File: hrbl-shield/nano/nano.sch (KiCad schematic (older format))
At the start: 57 parts, among them P1 Digital, P2 Analog, P3 CONN_01X01, P4 CONN_01X01, P5 CONN_01X01, P6 CONN_01X01, U1 SFH6206-3T, U10 SFH6206-3T, U11 SFH6206-3T, U12 SFH6206-3T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

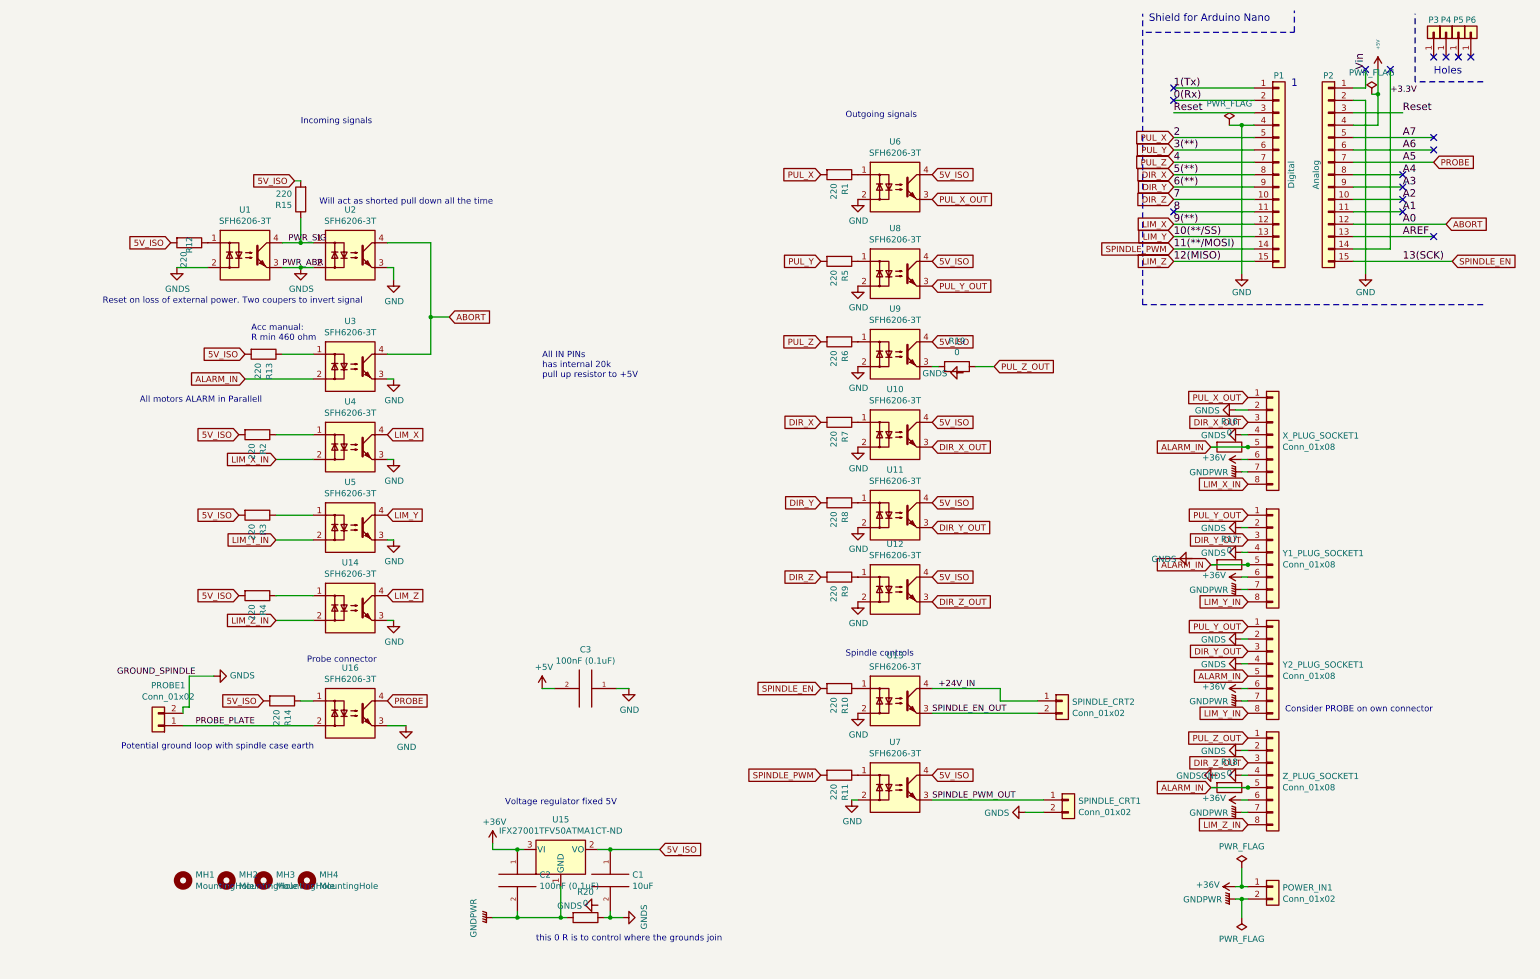
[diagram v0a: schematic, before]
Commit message: Dust skirt
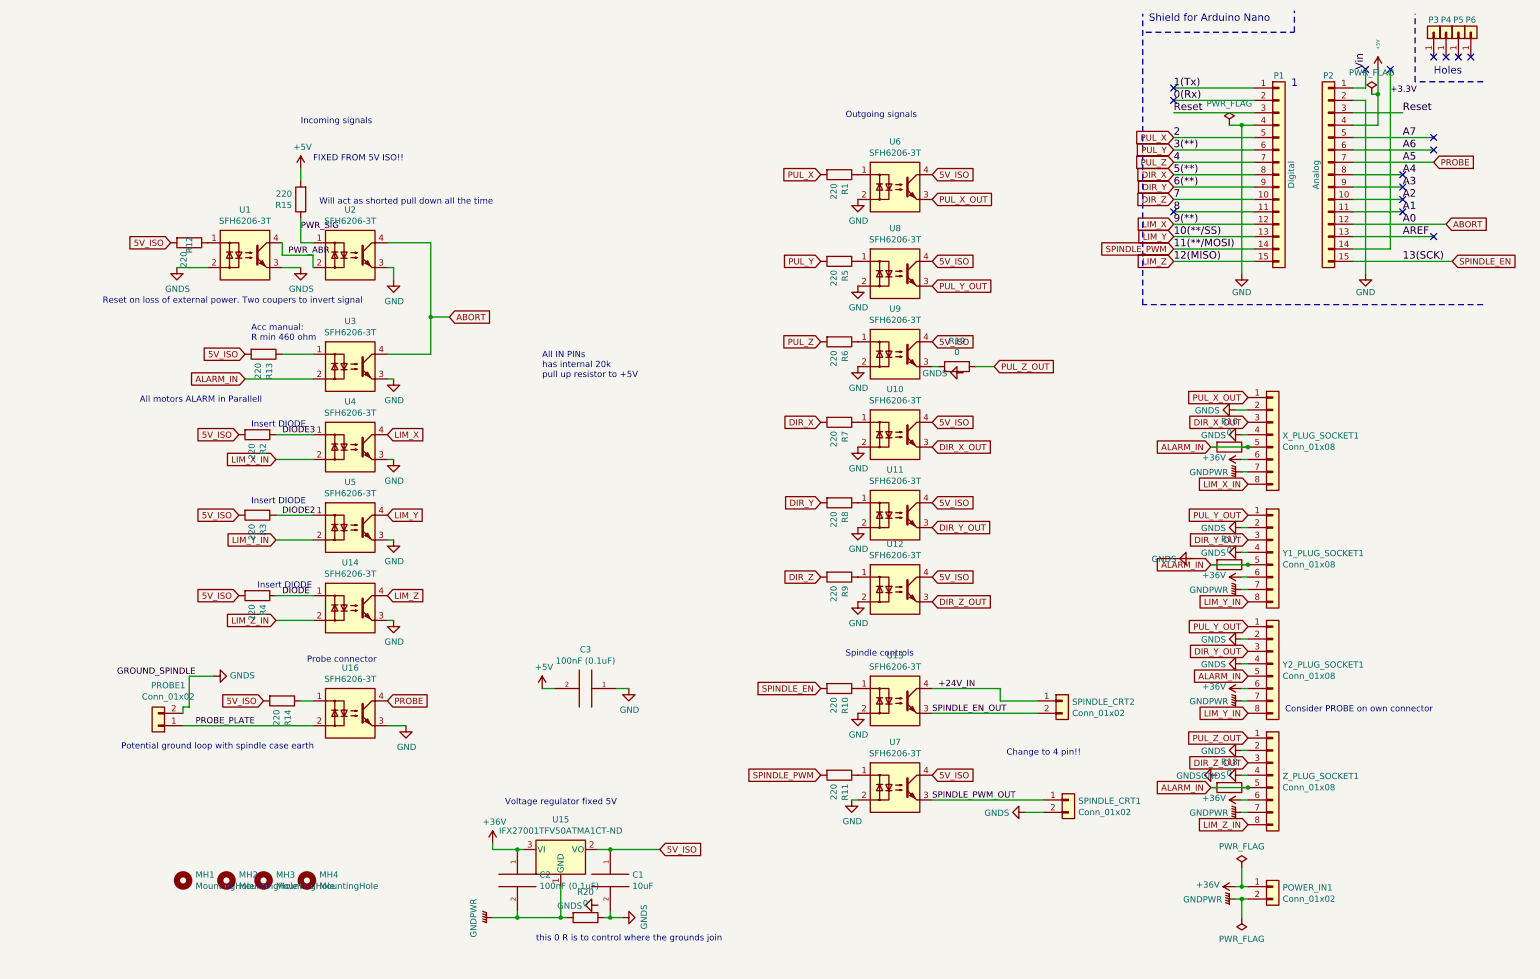
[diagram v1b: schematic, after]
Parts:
- Z_PLUG_SOCKET1: footprint Connector_Phoenix_MC:PhoenixContact_MCV_1,5_8-G-3.81_1x08_P3.81mm_Vertical -> Connector_Phoenix_MC:PhoenixContact_MCV_1,5_8-G-3.5_1x08_P3.50mm_Vertical
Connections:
- net +5V: now also R15.2
- net 5V_ISO: no longer R15.2
- net GNDS: no longer U2.2
- net PWR_SIG: no longer U1.4
- net DIODE3: now reaches R2.1, U4.1
- net DIODE2: now reaches R3.1, U5.1
- net DIODE: now reaches R4.1, U14.1
- new net PWR_ABR: U1.4, U2.2
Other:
- note added: "Change to 4 pin!!"
- note added: "FIXED FROM 5V ISO!!"
- note added: "Insert DIODE"
- note added: "Insert DIODE\n\n"
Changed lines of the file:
@@
 F 0 "Z_PLUG_SOCKET1" H 9579 6642 50  0000 L CNN
 F 1 "Conn_01x08" H 9579 6551 50  0000 L CNN
-F 2 "Connector_Phoenix_MC:PhoenixContact_MCV_1,5_8-G-3.81_1x08_P3.81mm_Vertical" H 9500 6650 50  0001 C CNN
+F 2 "Connector_Phoenix_MC:PhoenixContact_MCV_1,5_8-G-3.5_1x08_P3.50mm_Vertical" H 9500 6650 50  0001 C CNN
 F 3 "~" H 9500 6650 50  0001 C CNN
 	1    9500 6650
@@
 Wire Wire Line
 	2400 2550 2400 2650
-Text GLabel 1600 1850 0    50   Input ~ 0
-5V_ISO
 $Comp
 L Device:R R15
@@
 Acc manual: \nR min 460 ohm\n
 Wire Wire Line
-	1600 1850 1650 1850
-Wire Wire Line
 	1650 2150 1650 2350
 $Comp
@@
 $EndComp
 Wire Wire Line
-	1650 2350 1500 2350
-Wire Wire Line
 	650  2550 900  2550
 $Comp
@@
 $EndComp
 Wire Wire Line
-	1750 2550 1650 2550
-Connection ~ 1650 2550
-Wire Wire Line
 	1750 2350 1650 2350
-Connection ~ 1650 2350
 Wire Wire Line
 	2700 2350 2350 2350
@@
 Wire Wire Line
 	2350 4100 2400 4100
-Text Label 1500 2550 0    50   ~ 0
+Text Label 1550 2450 0    50   ~ 0
 PWR_ABR
-Text Label 1550 2350 0    50   ~ 0
+Text Label 1650 2250 0    50   ~ 0
 PWR_SIG
 $Comp
@@
 Wire Wire Line
 	750  5850 950  5850
+$Comp
+L power:+5V #PWR0115
+U 1 1 5B8E61E3
+P 1650 1750
+F 0 "#PWR0115" H 1650 1600 50  0001 C CNN
+F 1 "+5V" H 1665 1923 50  0000 C CNN
+F 2 "" H 1650 1750 50  0001 C CNN
+F 3 "" H 1650 1750 50  0001 C CNN
+	1    1650 1750
+	1    0    0    -1
+$EndComp
+Wire Wire Line
+	1650 1750 1650 1850
+Text Notes 1750 1700 0    50   ~ 0
+FIXED FROM 5V ISO!!
+Text Notes 7350 6500 0    50   ~ 0
+Change to 4 pin!!
+Text Notes 1300 5150 0    50   ~ 0
+Insert DIODE
+Text Notes 1250 4550 0    50   ~ 0
+Insert DIODE\n\n
+Text Notes 1250 3850 0    50   ~ 0
+Insert DIODE
+Text Label 1500 5200 0    50   ~ 0
+DIODE
+Text Label 1500 4550 0    50   ~ 0
+DIODE2
+Text Label 1500 3900 0    50   ~ 0
+DIODE3
+Wire Wire Line
+	1750 2550 1750 2450
+Wire Wire Line
+	1750 2450 1500 2450
+Wire Wire Line
+	1500 2450 1500 2350
 $EndSCHEMATC

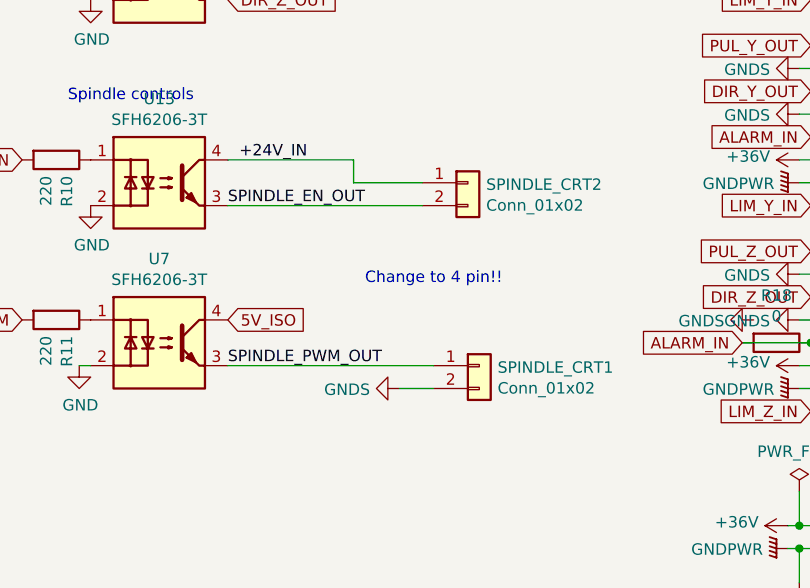
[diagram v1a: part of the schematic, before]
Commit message: corrected singals
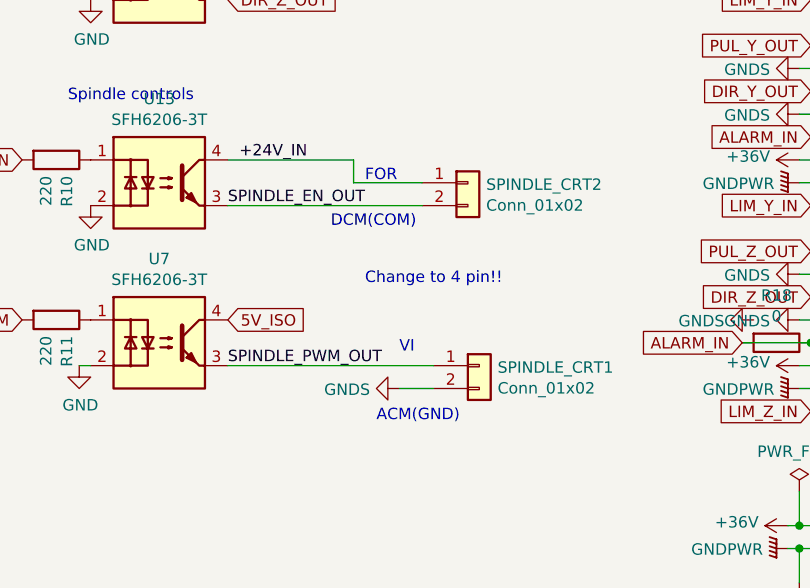
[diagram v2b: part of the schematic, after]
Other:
- note added: "ACM(GND)"
- note added: "DCM(COM)"
- note added: "FOR"
- note added: "VI\n"
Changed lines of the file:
@@
 Wire Wire Line
 	1500 2450 1500 2350
+Text Notes 7200 6250 0    50   ~ 0
+DCM(COM)
+Text Notes 7350 6050 0    50   ~ 0
+FOR
+Text Notes 7400 7100 0    50   ~ 0
+ACM(GND)
+Text Notes 7500 6800 0    50   ~ 0
+VI\n
 $EndSCHEMATC

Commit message: Shield fixes
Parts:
- removed SPINDLE_CRT1, SPINDLE_CRT2: Conn_01x02, Connector_Phoenix_MC:PhoenixContact_MCV_1,5_2-G-3.5_1x02_P3.50mm_Vertical, symbol Connector_Generic:Conn_01x02
- added J1: Conn_01x04, Connector_Phoenix_MC:PhoenixContact_MCV_1,5_4-G-3.5_1x04_P3.50mm_Vertical, symbol Connector_Generic:Conn_01x04
- added S1JA-13-F1: DIODE, Diode_SMD:D_SMA_Handsoldering, symbol pspice:DIODE
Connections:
- net 5V_ISO: now also S1JA-13-F1.1 (K); no longer R2.2, R3.2, R4.2
- net GNDS: now also J1.4 (Pin_4)
- net +24V_IN renamed FOR
- net FOR: now also J1.1 (Pin_1)
- net SPINDLE_EN_OUT renamed DCM(COM)
- net DCM(COM): now also J1.2 (Pin_2)
- net SPINDLE_PWM_OUT renamed VI
- net VI: now also J1.3 (Pin_3)
- new net: R2.2, R3.2, R4.2, S1JA-13-F1.2 (A)
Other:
- note added: "+24V in"
- note added: "Reset on loss of external power. \nTwo coupers to invert signal\n"
- note added: "Spindle PWM out"
- note added: "Spindle_EN_out"
- note added: "To stop backflow from the\n 36V pullup on the limit switch signal pin"
- note removed: "Change to 4 pin!!"
- note removed: "Reset on loss of external power. Two coupers to invert signal\n"
- note removed: "Will act as shorted pull down all the time"
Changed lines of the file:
@@
 Text Notes 6050 1350 0    50   ~ 0
 Outgoing signals
-Text Notes 1650 1400 0    50   ~ 0
-Incoming signals
 Text GLabel 2350 3900 2    50   Input ~ 0
 LIM_X
@@
 	1    2400 5400
 	1    0    0    -1
-$EndComp
-$Comp
-L Device:R R4
-U 1 1 5B816D2B
-P 1300 5200
-F 0 "R4" H 1370 5246 50  0000 L CNN
-F 1 "220" H 1370 5155 50  0000 L CNN
-F 2 "Resistor_SMD:R_1206_3216Metric_Pad1.42x1.75mm_HandSolder" V 1230 5200 50  0001 C CNN
-F 3 "~" H 1300 5200 50  0001 C CNN
-	1    1300 5200
-	0    1    1    0
 $EndComp
 $Comp
@@
 $EndComp
 Text Label 6800 5950 0    50   ~ 0
-+24V_IN
+FOR
 Text Label 6750 6150 0    50   ~ 0
-SPINDLE_EN_OUT
+DCM(COM)
 $Comp
 L power:GNDS #PWR06
 U 1 1 5B842985
-P 7500 6950
-F 0 "#PWR06" H 7500 6700 50  0001 C CNN
-F 1 "GNDS" V 7505 6822 50  0000 R CNN
-F 2 "" H 7500 6950 50  0001 C CNN
-F 3 "" H 7500 6950 50  0001 C CNN
-	1    7500 6950
+P 6800 6950
+F 0 "#PWR06" H 6800 6700 50  0001 C CNN
+F 1 "GNDS" V 6805 6822 50  0000 R CNN
+F 2 "" H 6800 6950 50  0001 C CNN
+F 3 "" H 6800 6950 50  0001 C CNN
+	1    6800 6950
 	0    1    1    0
 $EndComp
@@
 	1    0    0    -1
 $EndComp
-Text Label 6750 6850 0    50   ~ 0
-SPINDLE_PWM_OUT
 Text Notes 6050 5700 0    50   ~ 0
 Spindle controls
@@
 Text GLabel 6750 1800 2    50   Input ~ 0
 5V_ISO
-Text GLabel 1150 5200 0    50   Input ~ 0
-5V_ISO
-Text GLabel 1150 4550 0    50   Input ~ 0
-5V_ISO
-Text GLabel 1150 3900 0    50   Input ~ 0
+Text GLabel 150  4550 0    50   Input ~ 0
 5V_ISO
 Text GLabel 4550 7250 2    50   Input ~ 0
@@
 Text GLabel 2850 2950 2    50   Input ~ 0
 ABORT
-Text Notes 50   2850 0    50   ~ 0
-Reset on loss of external power. Two coupers to invert signal\n
+Text Notes 200  2950 0    50   ~ 0
+Reset on loss of external power. \nTwo coupers to invert signal\n
 Text Notes 3600 3450 0    50   ~ 0
 All IN PINs\nhas internal 20k \npull up resistor to +5V
@@
 	-1   0    0    1
 $EndComp
-Text Notes 1250 3150 0    50   ~ 0
+Text Notes 550  3400 0    50   ~ 0
 Acc manual: \nR min 460 ohm\n
 Wire Wire Line
@@
 L power:GNDS #PWR08
 U 1 1 5B9C09BB
-P 1650 2550
-F 0 "#PWR08" H 1650 2300 50  0001 C CNN
-F 1 "GNDS" H 1655 2377 50  0000 C CNN
-F 2 "" H 1650 2550 50  0001 C CNN
-F 3 "" H 1650 2550 50  0001 C CNN
-	1    1650 2550
+P 1650 2600
+F 0 "#PWR08" H 1650 2350 50  0001 C CNN
+F 1 "GNDS" H 1655 2427 50  0000 C CNN
+F 2 "" H 1650 2600 50  0001 C CNN
+F 3 "" H 1650 2600 50  0001 C CNN
+	1    1650 2600
 	1    0    0    -1
 $EndComp
@@
 Wire Wire Line
 	4200 5950 4300 5950
-Text Notes 1800 2050 0    50   ~ 0
-Will act as shorted pull down all the time
 $Comp
 L Isolator:SFH6206-3T U6
@@
 	1    0    0    -1
 $EndComp
-Wire Wire Line
-	6750 5950 7300 5950
-Wire Wire Line
-	7300 5950 7300 6050
 $Comp
 L Isolator:SFH6206-3T U7
@@
 	1    0    0    -1
 $EndComp
-$Comp
-L Connector_Generic:Conn_01x02 SPINDLE_CRT2
-U 1 1 5B881667
-P 7800 6050
-F 0 "SPINDLE_CRT2" H 7880 6042 50  0000 L CNN
-F 1 "Conn_01x02" H 7880 5951 50  0000 L CNN
-F 2 "Connector_Phoenix_MC:PhoenixContact_MCV_1,5_2-G-3.5_1x02_P3.50mm_Vertical" H 7800 6050 50  0001 C CNN
-F 3 "~" H 7800 6050 50  0001 C CNN
-	1    7800 6050
-	1    0    0    -1
-$EndComp
-$Comp
-L Connector_Generic:Conn_01x02 SPINDLE_CRT1
-U 1 1 5B887DAA
-P 7850 6850
-F 0 "SPINDLE_CRT1" H 7930 6842 50  0000 L CNN
-F 1 "Conn_01x02" H 7930 6751 50  0000 L CNN
-F 2 "Connector_Phoenix_MC:PhoenixContact_MCV_1,5_2-G-3.5_1x02_P3.50mm_Vertical" H 7850 6850 50  0001 C CNN
-F 3 "~" H 7850 6850 50  0001 C CNN
-	1    7850 6850
-	1    0    0    -1
-$EndComp
-Wire Wire Line
-	7300 6050 7600 6050
-Wire Wire Line
-	6750 6150 7600 6150
 Wire Wire Line
 	6750 6850 7650 6850
-Wire Wire Line
-	7500 6950 7650 6950
 Text Label 800  5850 2    50   ~ 0
 GROUND_SPINDLE
@@
 Text Notes 1750 1700 0    50   ~ 0
 FIXED FROM 5V ISO!!
-Text Notes 7350 6500 0    50   ~ 0
-Change to 4 pin!!
 Text Notes 1300 5150 0    50   ~ 0
 Insert DIODE
@@
 Wire Wire Line
 	1500 2450 1500 2350
-Text Notes 7200 6250 0    50   ~ 0
+Text Notes 8250 6450 0    50   ~ 0
 DCM(COM)
-Text Notes 7350 6050 0    50   ~ 0
+Text Notes 8250 6350 0    50   ~ 0
 FOR
-Text Notes 7400 7100 0    50   ~ 0
+Text Notes 8250 6650 0    50   ~ 0
 ACM(GND)
-Text Notes 7500 6800 0    50   ~ 0
+Text Notes 8250 6550 0    50   ~ 0
 VI\n
+$Comp
+L pspice:DIODE S1JA-13-F1
+U 1 1 5B92F59F
+P 400 4550
+F 0 "S1JA-13-F1" H 400 4815 50  0000 C CNN
+F 1 "DIODE" H 400 4724 50  0000 C CNN
+F 2 "Diode_SMD:D_SMA_Handsoldering" H 400 4550 50  0001 C CNN
+F 3 "https://www.diodes.com/assets/Datasheets/ds16003.pdf" H 400 4550 50  0001 C CNN
+	1    400  4550
+	1    0    0    -1
+$EndComp
+$Comp
+L Device:R R4
+U 1 1 5B816D2B
+P 1300 5200
+F 0 "R4" H 1370 5246 50  0000 L CNN
+F 1 "220" H 1370 5155 50  0000 L CNN
+F 2 "Resistor_SMD:R_1206_3216Metric_Pad1.42x1.75mm_HandSolder" V 1230 5200 50  0001 C CNN
+F 3 "~" H 1300 5200 50  0001 C CNN
+	1    1300 5200
+	0    1    1    0
+$EndComp
+Wire Wire Line
+	1150 3900 700  3900
+Wire Wire Line
+	1150 5200 700  5200
+Wire Wire Line
+	700  3900 700  4550
+Wire Wire Line
+	1150 4550 700  4550
+Connection ~ 700  4550
+Wire Wire Line
+	700  4550 700  5200
+Wire Wire Line
+	600  4550 700  4550
+Wire Wire Line
+	150  4550 200  4550
+Text Notes -700 4800 0    50   ~ 0
+To stop backflow from the\n 36V pullup on the limit switch signal pin
+Text Notes 1400 950  0    50   ~ 0
+Incoming signals
+Wire Notes Line
+	1500 2350 1650 2350
+Wire Notes Line
+	1650 2550 1750 2550
+Wire Wire Line
+	1650 2600 1650 2550
+$Comp
+L Connector_Generic:Conn_01x04 J1
+U 1 1 5B97B5A1
+P 8150 6400
+F 0 "J1" H 8230 6392 50  0000 L CNN
+F 1 "Conn_01x04" H 8230 6301 50  0000 C BNN
+F 2 "Connector_Phoenix_MC:PhoenixContact_MCV_1,5_4-G-3.5_1x04_P3.50mm_Vertical" H 8150 6400 50  0001 C CNN
+F 3 "~" H 8150 6400 50  0001 C CNN
+	1    8150 6400
+	1    0    0    -1
+$EndComp
+Wire Wire Line
+	6750 6150 7650 6150
+Wire Wire Line
+	7650 6850 7650 6500
+Wire Wire Line
+	7650 6500 7950 6500
+Wire Wire Line
+	7750 6950 7750 6600
+Wire Wire Line
+	7750 6600 7950 6600
+Wire Wire Line
+	7650 6400 7650 6150
+Wire Wire Line
+	7650 6400 7950 6400
+Wire Wire Line
+	7950 6300 7750 6300
+Text Notes 7150 6150 0    50   ~ 0
+Spindle_EN_out
+Text Notes 6950 5950 0    50   ~ 0
++24V in
+Text Notes 6850 6850 0    50   ~ 0
+Spindle PWM out
+Text Label 6750 6850 0    50   ~ 0
+VI
+Text Label 6900 6950 0    50   ~ 0
+ACM(GND)
+Wire Wire Line
+	6750 5950 7750 5950
+Wire Wire Line
+	7750 5950 7750 6300
+Wire Wire Line
+	6800 6950 7750 6950
 $EndSCHEMATC

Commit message: nano and logo
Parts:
- added R21, R22: 220, Resistor_SMD:R_1206_3216Metric_Pad1.42x1.75mm_HandSolder, symbol Device:R
- added S1JA-13-F2, S1JA-13-F3: DIODE, Diode_SMD:D_SMA_Handsoldering, symbol pspice:DIODE
- renumbered J1 to SPINDLE1
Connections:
- net PWR_SIG is gone; now on an unnamed net: R15.1, U2.1
- net +5V: now also R21.2
- net 5V_ISO: now also S1JA-13-F2.1 (K), S1JA-13-F3.1 (K)
- net ABORT: now also R22.1
- net GNDS: now also U2.2
- net at R2.2, S1JA-13-F1.2 (A): no longer R3.2, R4.2
- net DIODE: no longer names the net of R4.1, U14.1
- net DIODE2: no longer names the net of R3.1, U5.1
- net DIODE3: no longer names the net of R2.1, U4.1
- net PWR_ABR: no longer names the net of U1.4
- net PWR_ABR: no longer U2.2
- new net: R3.2, S1JA-13-F2.2 (A)
- new net: R4.2, S1JA-13-F3.2 (A)
- new net: R21.1, R22.2
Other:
- note added: "Diodes to stop backflow from the\n 36V pullup on the limit switch signal pin"
- note added: "From arduino"
- note added: "From regulator"
- note added: "Optional. Adds to\nInternal 20k pull up"
- note removed: "Acc manual: \nR min 460 ohm\n"
- note removed: "Consider PROBE on own connector\n"
- note removed: "FIXED FROM 5V ISO!!"
- note removed: "Insert DIODE"
- note removed: "Insert DIODE\n\n"
- note removed: "Reset on loss of external power. \nTwo coupers to invert signal\n"
- note removed: "To stop backflow from the\n 36V pullup on the limit switch signal pin"
- moved on the sheet: R12, R15, S1JA-13-F1, U1, U2
